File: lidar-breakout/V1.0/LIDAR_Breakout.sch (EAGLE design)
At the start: 95 parts, among them P1 MOLEX 0436500200, X1 TSX-3225 16.0000MF18X-AC0

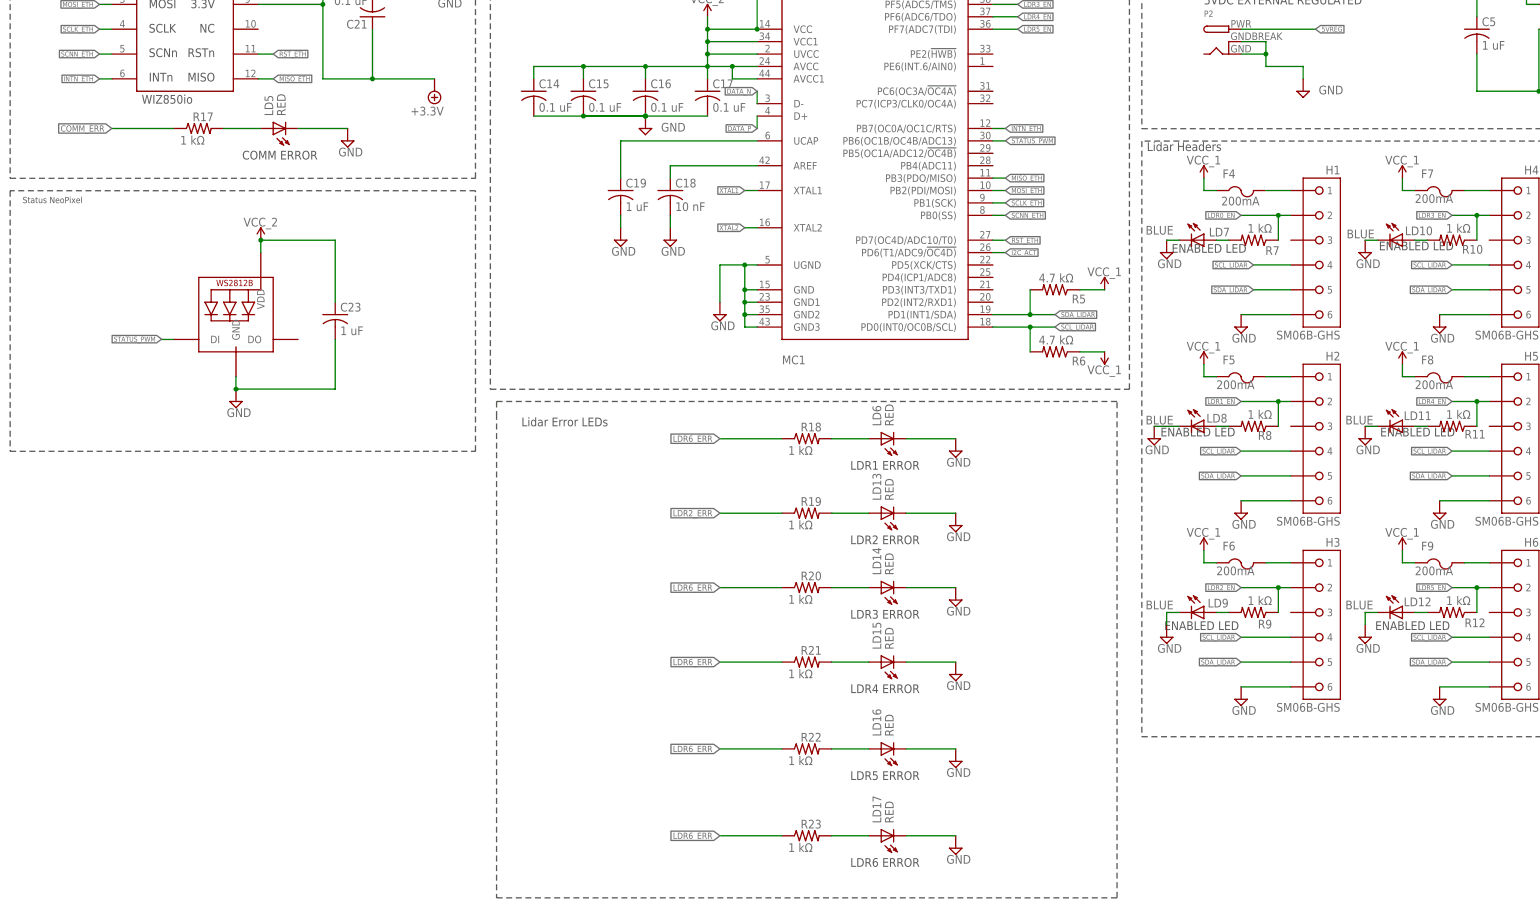
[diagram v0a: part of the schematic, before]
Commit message: Branch Cleanup, Rev 1.1 Updates
Added I2C IO expander and resistor array for new leds.
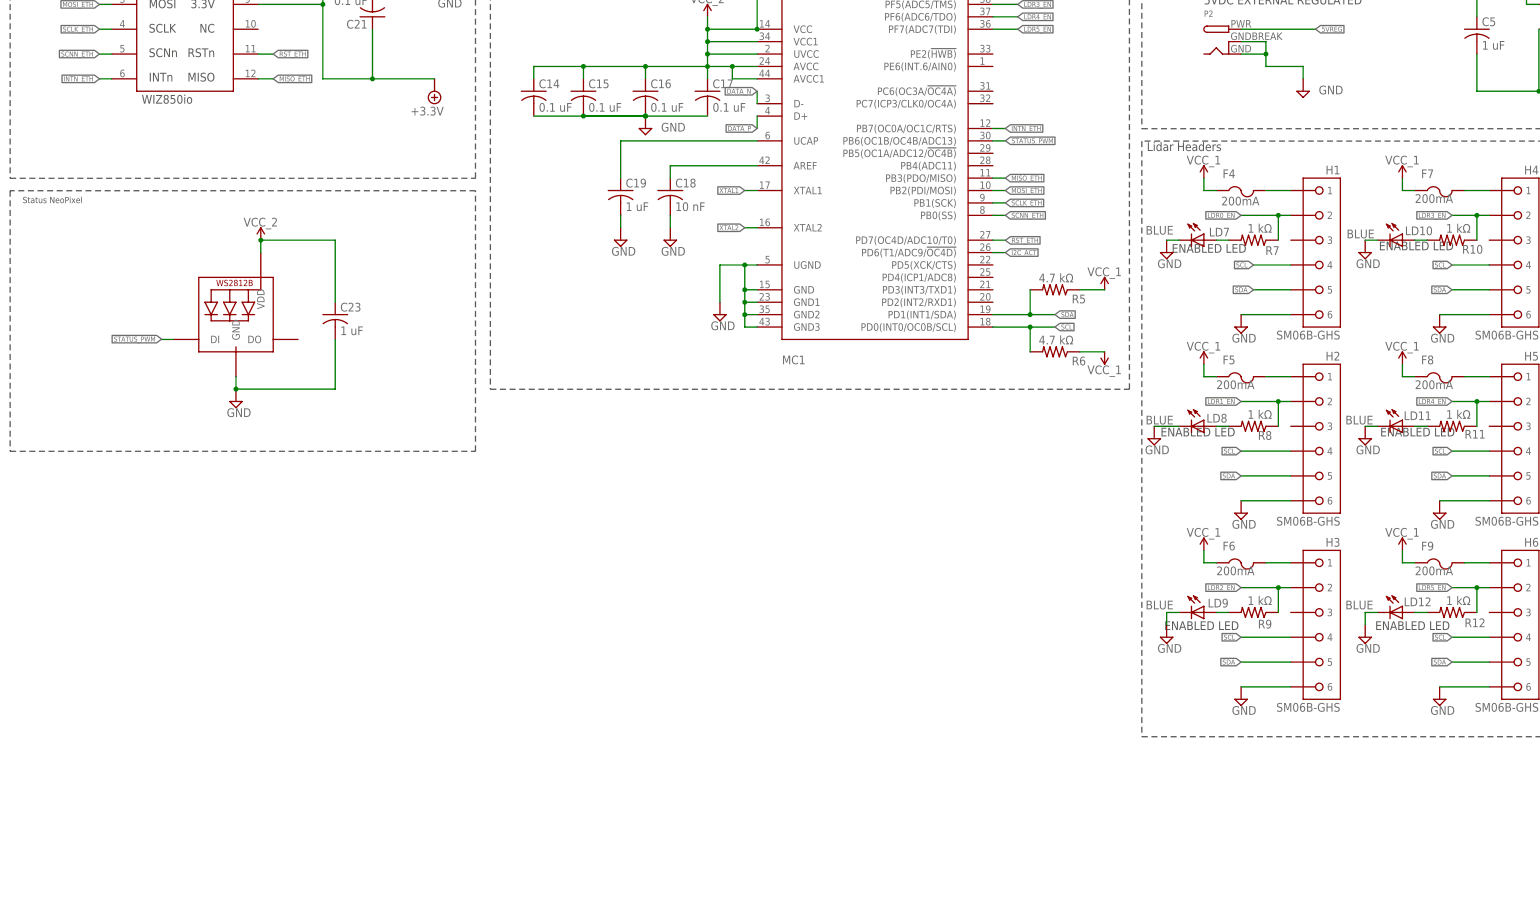
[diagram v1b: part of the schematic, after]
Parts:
- removed LD13, LD14, LD15, LD16, LD17, LD5, LD6: RED, RoboJackets-LEDs:LED-SMD-RED
- removed R17, R18, R19, R20, R21, R22, R23: 1 kΩ, rcl:R-US_R0603
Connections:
- net SCL_LIDAR renamed SCL
- net SDA_LIDAR renamed SDA
- removed net COMM_ERR: R17.1
- removed net LDR2_ERR: R19.1
- removed net LDR6_ERR: R18.1, R20.1, R21.1, R22.1, R23.1
- removed net N$10: LD6.A, R18.2
- removed net N$11: LD13.A, R19.2
- removed net N$12: LD14.A, R20.2
- removed net N$13: LD15.A, R21.2
- removed net N$14: LD16.A, R22.2
- removed net N$15: LD17.A, R23.2
- removed net N$9: LD5.A, R17.2
- net GND: no longer LD13.K, LD14.K, LD15.K, LD16.K, LD17.K, LD5.K, LD6.K
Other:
- note removed: "COMM ERROR"
- note removed: "LDR1 ERROR"
- note removed: "LDR2 ERROR"
- note removed: "LDR3 ERROR"
- note removed: "LDR4 ERROR"
- note removed: "LDR5 ERROR"
- note removed: "LDR6 ERROR"
- note removed: "Lidar Error LEDs"
